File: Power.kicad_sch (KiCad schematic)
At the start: 22 parts, among them T1 Transformer_1P_1S

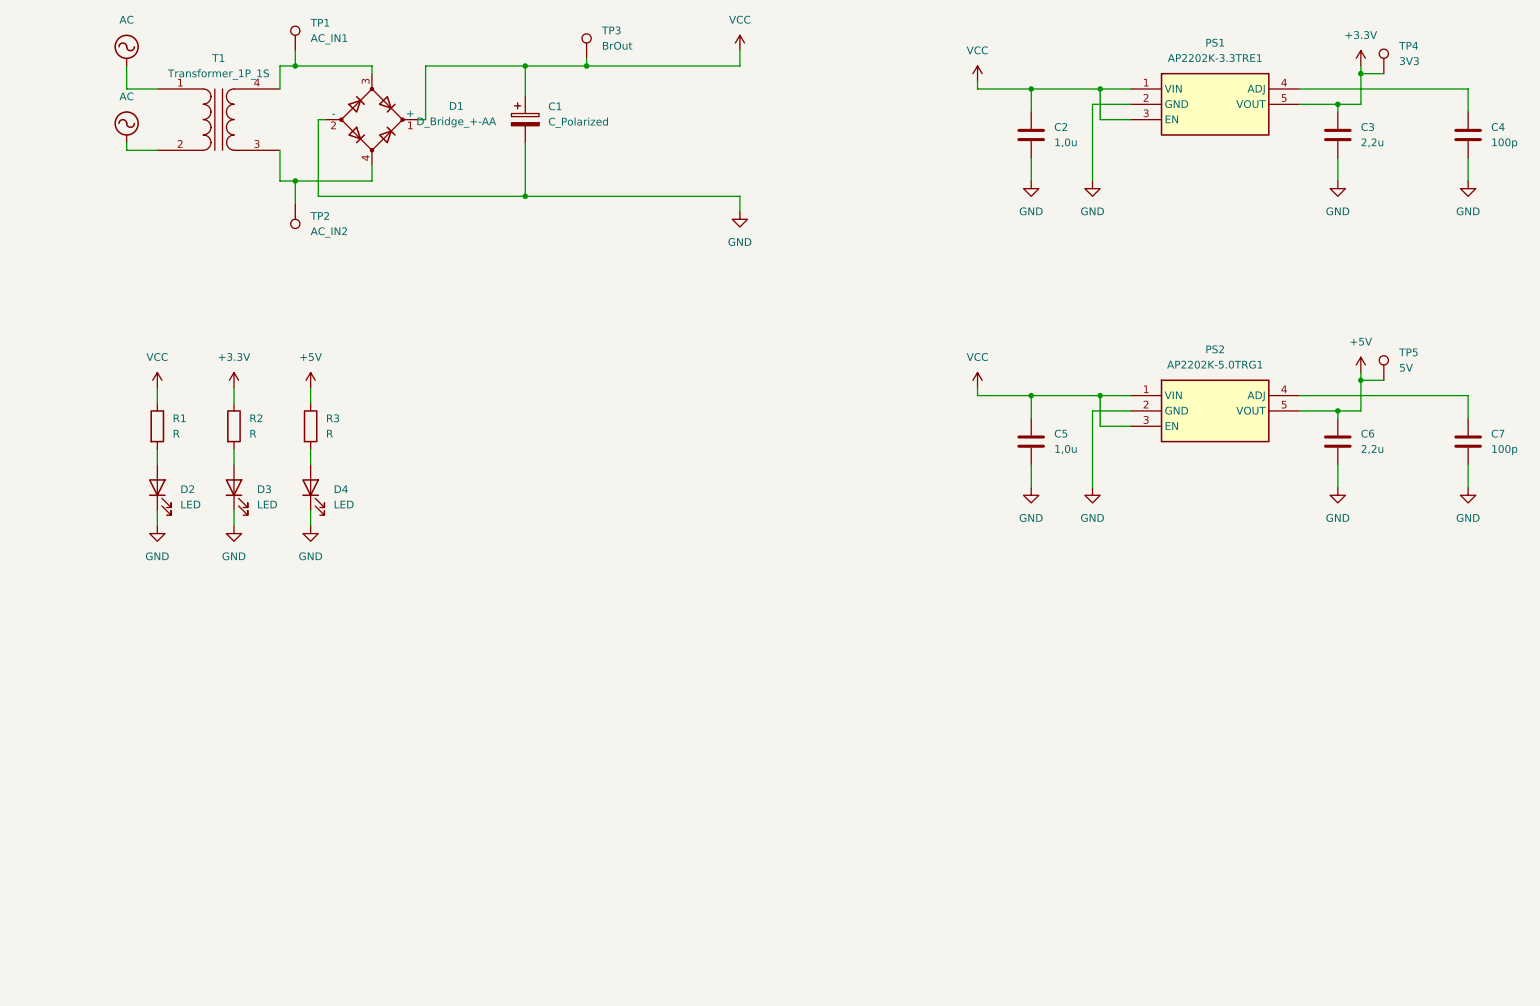
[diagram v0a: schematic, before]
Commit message: Power update - DC/DC Converter
Updated the power source to be done on the DC/DC Converter
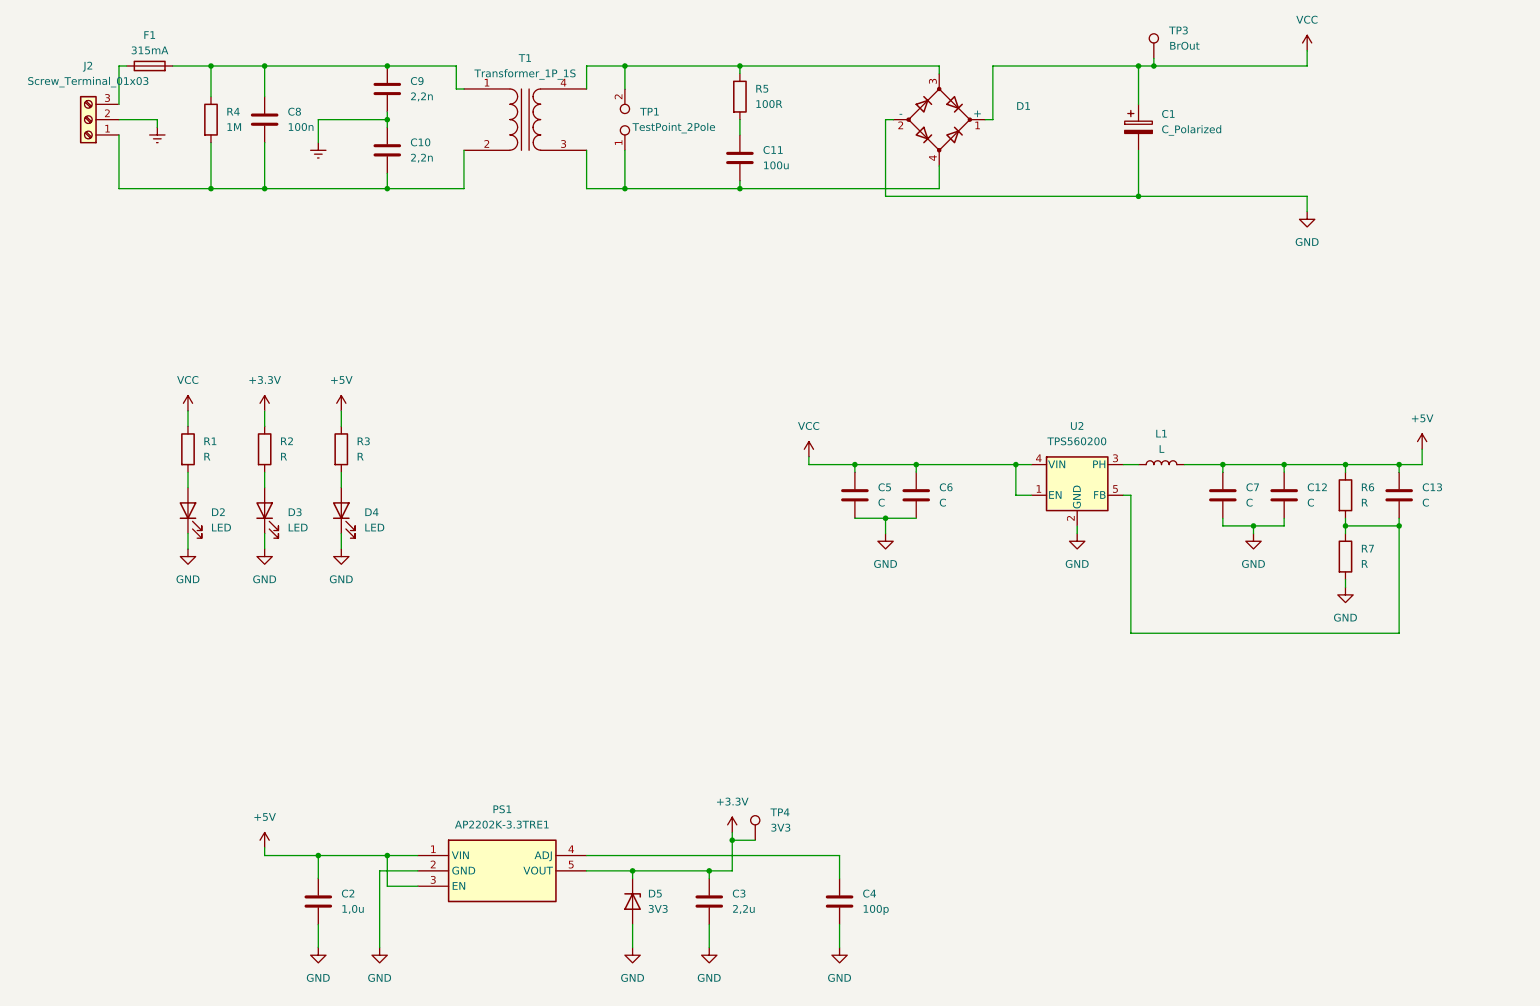
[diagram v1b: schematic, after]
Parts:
- removed PS2: AP2202K-5.0TRG1, SOT95P280X145-5N, symbol LibLoader:AP2202K-ADJTRG1
- removed TP1: AC_IN1, symbol Connector:TestPoint
- removed TP2: AC_IN2, symbol Connector:TestPoint
- removed TP5: 5V, symbol Connector:TestPoint
- added C10, C9: 2,2n, symbol Device:C
- added C11: 100u, symbol Device:C
- added C12, C13: C, symbol Device:C
- added C8: 100n, symbol Device:C
- added D5: 3V3, symbol Device:D_Zener
- added F1: 315mA, symbol Device:Fuse
- added J2: Screw_Terminal_01x03, symbol Connector:Screw_Terminal_01x03
- added L1: L, symbol Device:L
- added R4: 1M, symbol Device:R
- added R5: 100R, symbol Device:R
- added R6, R7: R, symbol Device:R
- added TP1: TestPoint_2Pole, symbol Connector:TestPoint_2Pole
- added U2: TPS560200, Package_TO_SOT_SMD:SOT-23-5, symbol Regulator_Switching:TPS560200
- C5: value 1,0u -> C
- C6: value 2,2u -> C
- C7: value 100p -> C
- D1: value D_Bridge_+-AA -> MB8FTR
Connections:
- net +3.3V: now also D5.1 (K)
- net +5V: now also C2.1, C7.1, PS1.1 (VIN), PS1.3 (EN), C12.1, C13.1, L1.2, R6.1; no longer C6.1
- net GND: now also C12.2, D5.2 (A), R7.2, U2.2 (GND)
- net VCC: now also C6.1, U2.1 (EN), U2.4 (VIN); no longer C2.1, PS1.1 (VIN), PS1.3 (EN)
- net at D1.3, T1.4 (SB): now also R5.1, TP1.2
- net at D1.4, T1.3 (SA): now also C11.2, TP1.1
- net AC: no longer names the net of T1.1 (AA)
- net AC: now also C8.1, C9.1, F1.2, R4.1; no longer T1.2 (AB)
- new net: C11.1, R5.2
- new net: C13.2, R6.2, R7.1, U2.5 (FB)
- new net: C10.2, C8.2, J2.1 (Pin_1), R4.2, T1.2 (AB)
- new net: L1.1, U2.3 (PH)
- new net: F1.1, J2.3 (Pin_3)
- new net Earth: C10.1, C9.2, J2.2 (Pin_2)
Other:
- moved on the sheet: C1, C2, C3, C4, D1, D2, D3, D4, PS1, R1, R2, R3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

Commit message: Microcontroller draft
Created a draft of the things connected to the microcontroller.
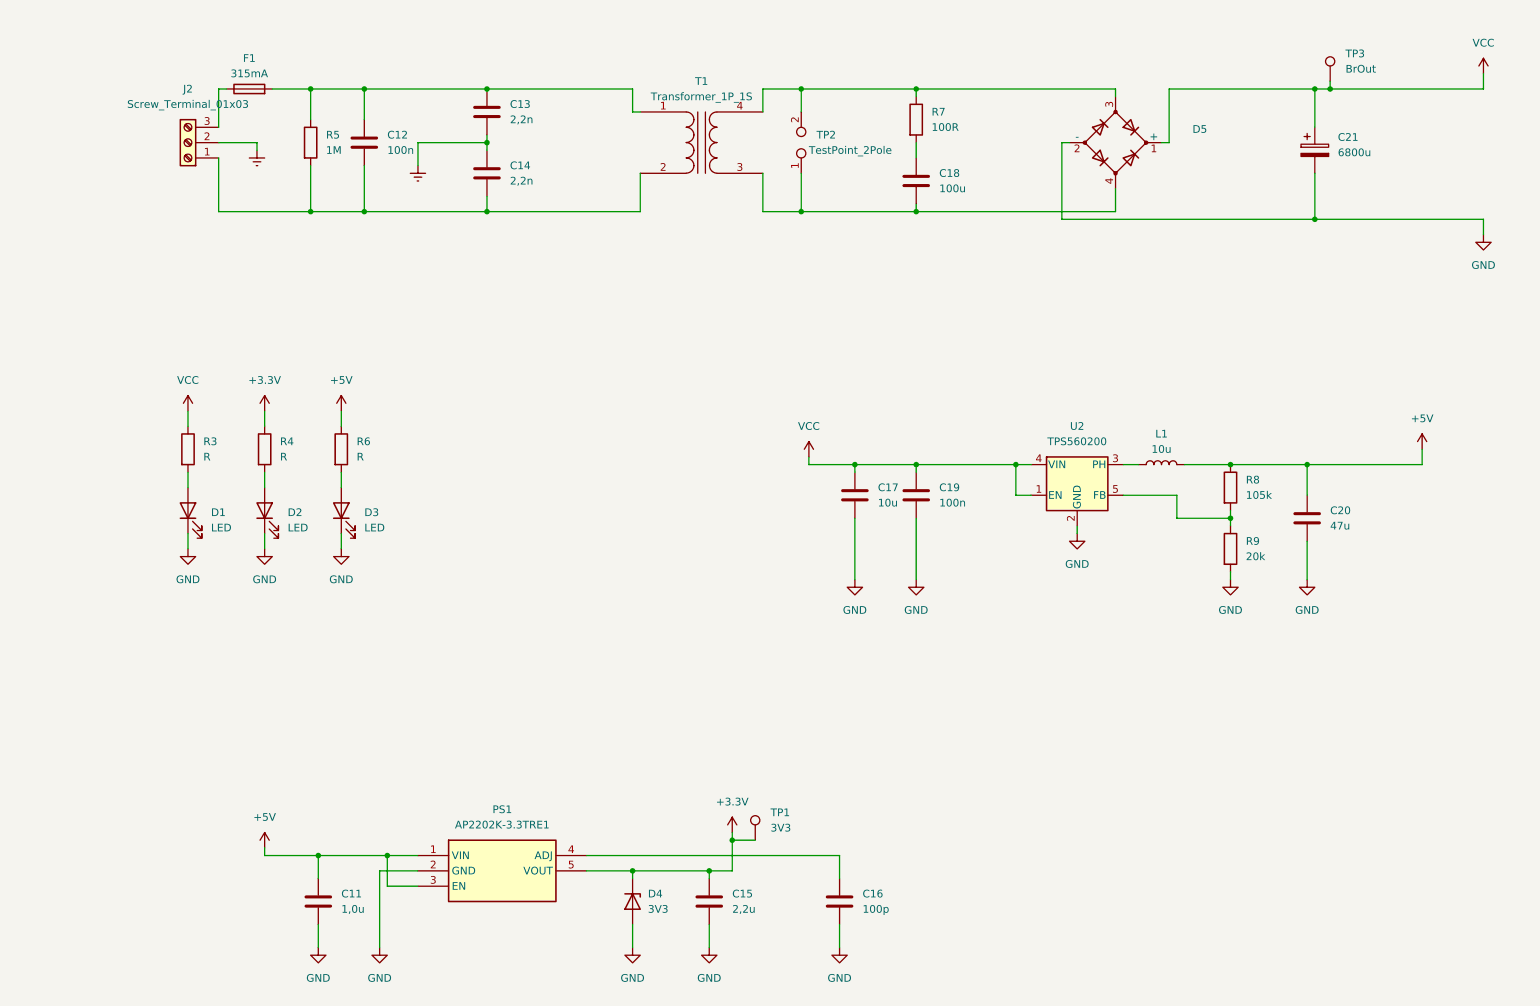
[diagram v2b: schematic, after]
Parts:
- removed C12, C13, C7: C, symbol Device:C
- added C20: 47u, symbol Device:C
- C17: renamed from C5; value C -> 10u
- C19: renamed from C6; value C -> 100n
- C21: renamed from C1; value C_Polarized -> 6800u
- L1: value L -> 10u
- R8: renamed from R6; value R -> 105k
- R9: renamed from R7; value R -> 20k
- renumbered C2 to C11, C8 to C12, C9 to C13, C10 to C14, C3 to C15, C4 to C16, C11 to C18, D2 to D1, D3 to D2, D4 to D3, D5 to D4, D1 to D5, R1 to R3, R2 to R4, R4 to R5, R3 to R6, R5 to R7, TP4 to TP1, TP1 to TP2
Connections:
- net +5V: now also C20.1
- net GND: now also C20.2
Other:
- moved on the sheet: C12, C13, C14, C18, C21, D5, F1, J2, R5, R7, R8, R9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

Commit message: Partial measurement block
Added capacitor in Power, fixed the debug junction, added initial draft of measurement block
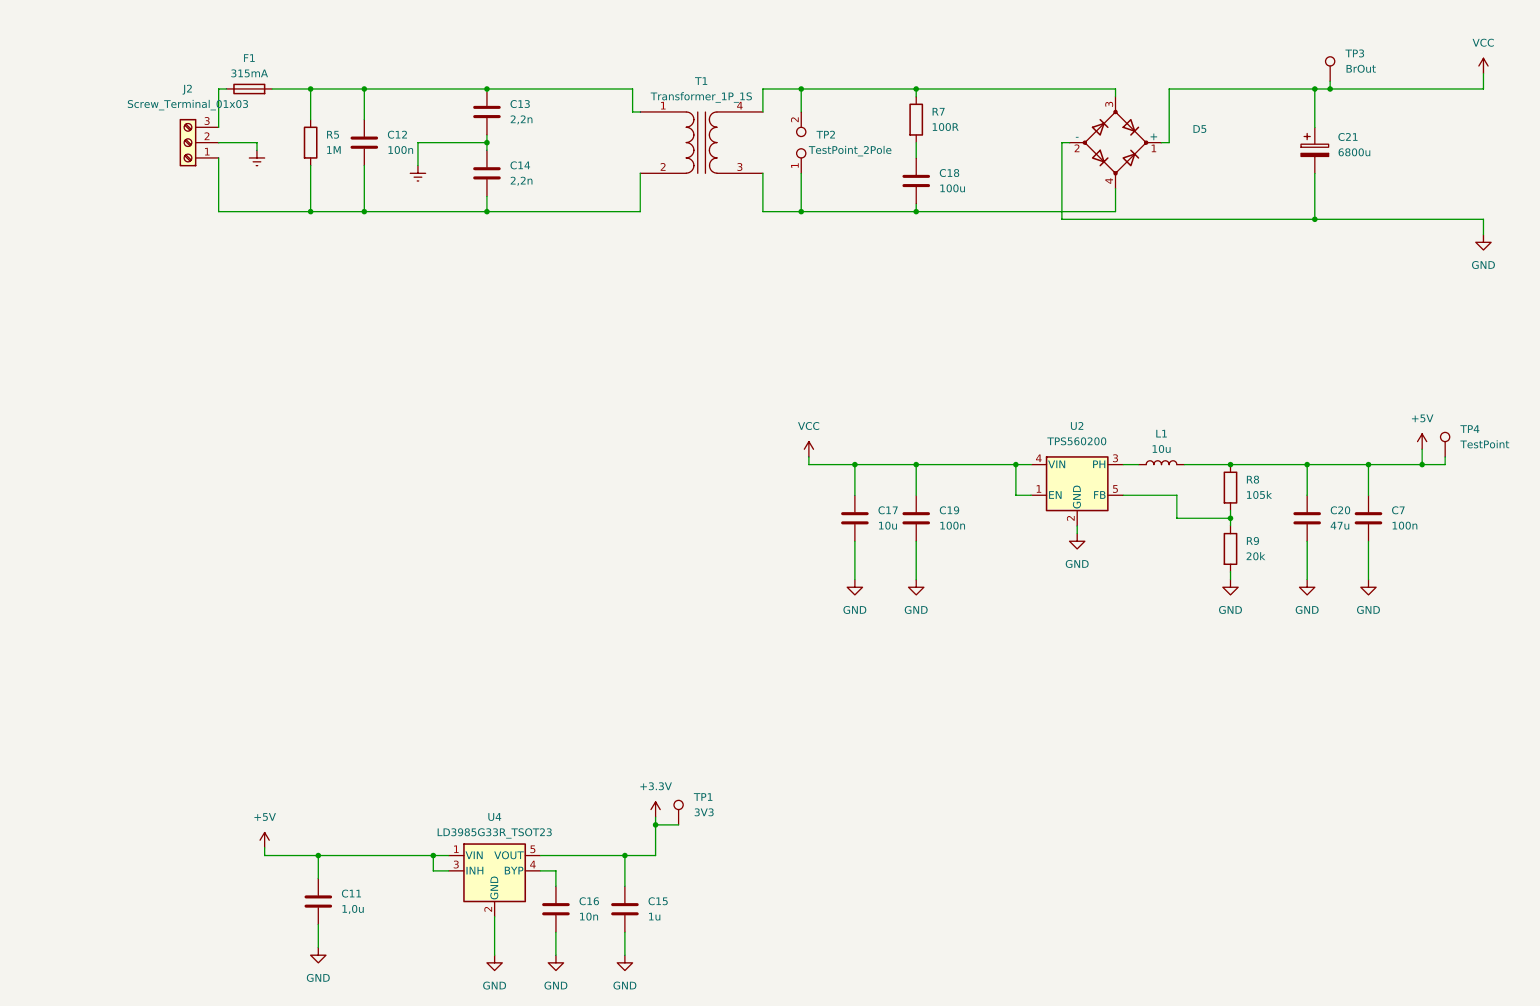
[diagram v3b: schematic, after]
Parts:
- removed D1, D2, D3: LED, symbol Device:LED
- removed D4: 3V3, symbol Device:D_Zener
- removed PS1: AP2202K-3.3TRE1, SOT95P280X145-5N, symbol LibLoader:AP2202K-ADJTRG1
- removed R3, R4, R6: R, symbol Device:R
- added C7: 100n, symbol Device:C
- added TP4: TestPoint, symbol Connector:TestPoint
- added U4: LD3985G33R_TSOT23, Package_TO_SOT_SMD:TSOT-23-5, symbol Regulator_Linear:LD3985G33R_TSOT23
- C15: value 2,2u -> 1u
- C16: value 100p -> 10n
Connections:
- net +3.3V: now also U4.5 (VOUT)
- net +5V: now also C7.1, TP4.1, U4.1 (VIN), U4.3 (INH)
- net GND: now also C7.2, U4.2 (GND)
- net at C16.1: now also U4.4 (BYP)
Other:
- moved on the sheet: C15, C17, C19, TP1
